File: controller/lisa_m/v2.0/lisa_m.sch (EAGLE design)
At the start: 119 parts, among them IC9 LP2992 5V, J1 CONN_3-1, J2 CONN_3-1, J3 CONN_3-1, J4 CONN_3-1, J5 CONN_3-1, J6 CONN_3-1, J7 CONN_3-1, J8 CONN_3-1, Q1 12Mhz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

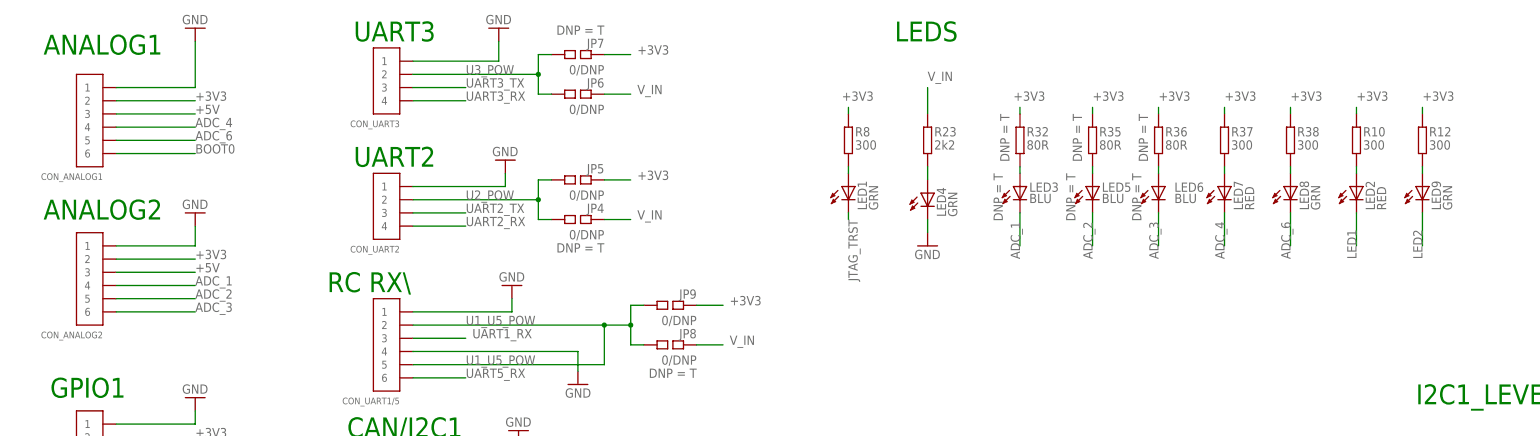
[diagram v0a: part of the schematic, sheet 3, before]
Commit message: - switched analog1 and analog2 connector labels on schematic and silkscreen  - changed LED labels on schematic to be more intuitive and match software defines  - changed power led to LEDVIN from LED4 (can't be controlled) in schematic  - changed LED silkscreen label numbers to match new schematic labels
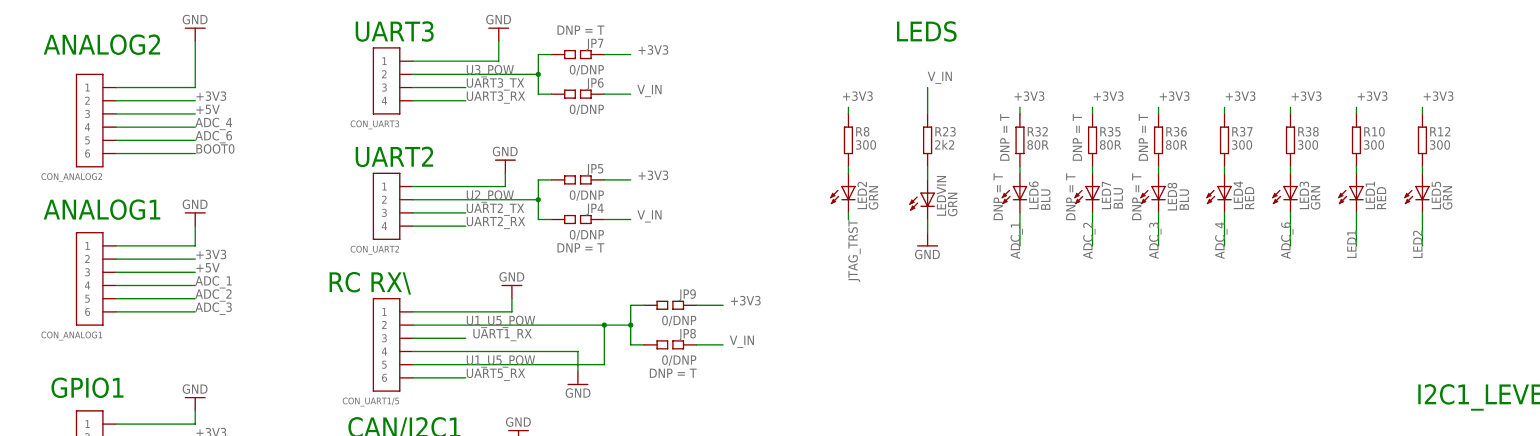
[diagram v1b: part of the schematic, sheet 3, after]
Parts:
- removed LED9: GRN, pel_dipol_comp:LED-0402
- added LEDVIN: GRN, pel_dipol_comp:LED-0402
- LED1, LED4: value GRN -> RED; PARTNO led-0402-green -> led-0402-red
- LED2: value RED -> GRN; PARTNO led-0402-red -> led-0402-green
- LED3, LED5: value BLU -> GRN; DNP T -> (none); PARTNO led-0402-blue -> led-0402-green
- LED7: value RED -> BLU; DNP (none) -> T; PARTNO led-0402-red -> led-0402-blue
- LED8: value GRN -> BLU; DNP (none) -> T; PARTNO led-0402-green -> led-0402-blue
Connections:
- net ADC_1: now also CON_ANALOG1.4, LED6.C; no longer CON_ANALOG2.4, LED3.C
- net ADC_2: now also CON_ANALOG1.5, LED7.C; no longer CON_ANALOG2.5, LED5.C
- net ADC_3: now also CON_ANALOG1.6, LED8.C; no longer CON_ANALOG2.6, LED6.C
- net ADC_4: now also CON_ANALOG2.4, LED4.C; no longer CON_ANALOG1.4, LED7.C
- net ADC_6: now also CON_ANALOG2.5, LED3.C; no longer CON_ANALOG1.5, LED8.C
- net BOOT0: now also CON_ANALOG2.6; no longer CON_ANALOG1.6
- net GND: now also LEDVIN.C; no longer LED4.C
- net JTAG_TRST: now also LED2.C; no longer LED1.C
- net LED1: now also LED1.C; no longer LED2.C
- net LED2: now also LED5.C; no longer LED9.C
- net N$10: now also LED2.A; no longer LED1.A
- net N$11: now also LED8.A; no longer LED6.A
- net N$12: now also LEDVIN.A; no longer LED4.A
- net N$13: now also LED5.A; no longer LED9.A
- net N$14: now also LED4.A; no longer LED7.A
- net N$15: now also LED3.A; no longer LED8.A
- net N$4: now also LED1.A; no longer LED2.A
- net N$5: now also LED6.A; no longer LED3.A
- net N$9: now also LED7.A; no longer LED5.A
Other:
- moved on the sheet: CON_ANALOG1, CON_ANALOG2, LED1, LED2, LED3, LED4, LED5, LED6, LED7, LED8
